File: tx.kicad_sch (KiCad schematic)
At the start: 58 parts, among them Q10 MMBF170, Q11 MMBF170, Q12 MMBF170, Q13 MMBF170, Q2 MMBF170, Q3 MMBF170, Q4 MMBF170, Q5 MMBF170, Q6 MMBF170, Q7 MMBF170, Q8 MMBF170, Q9 MMBF170, T1 BN-43-202_DualPri_CTSec, U4 ICE40UP5K-SG48ITR, U5 TLV70012, U6 CD74ACT541M96G4

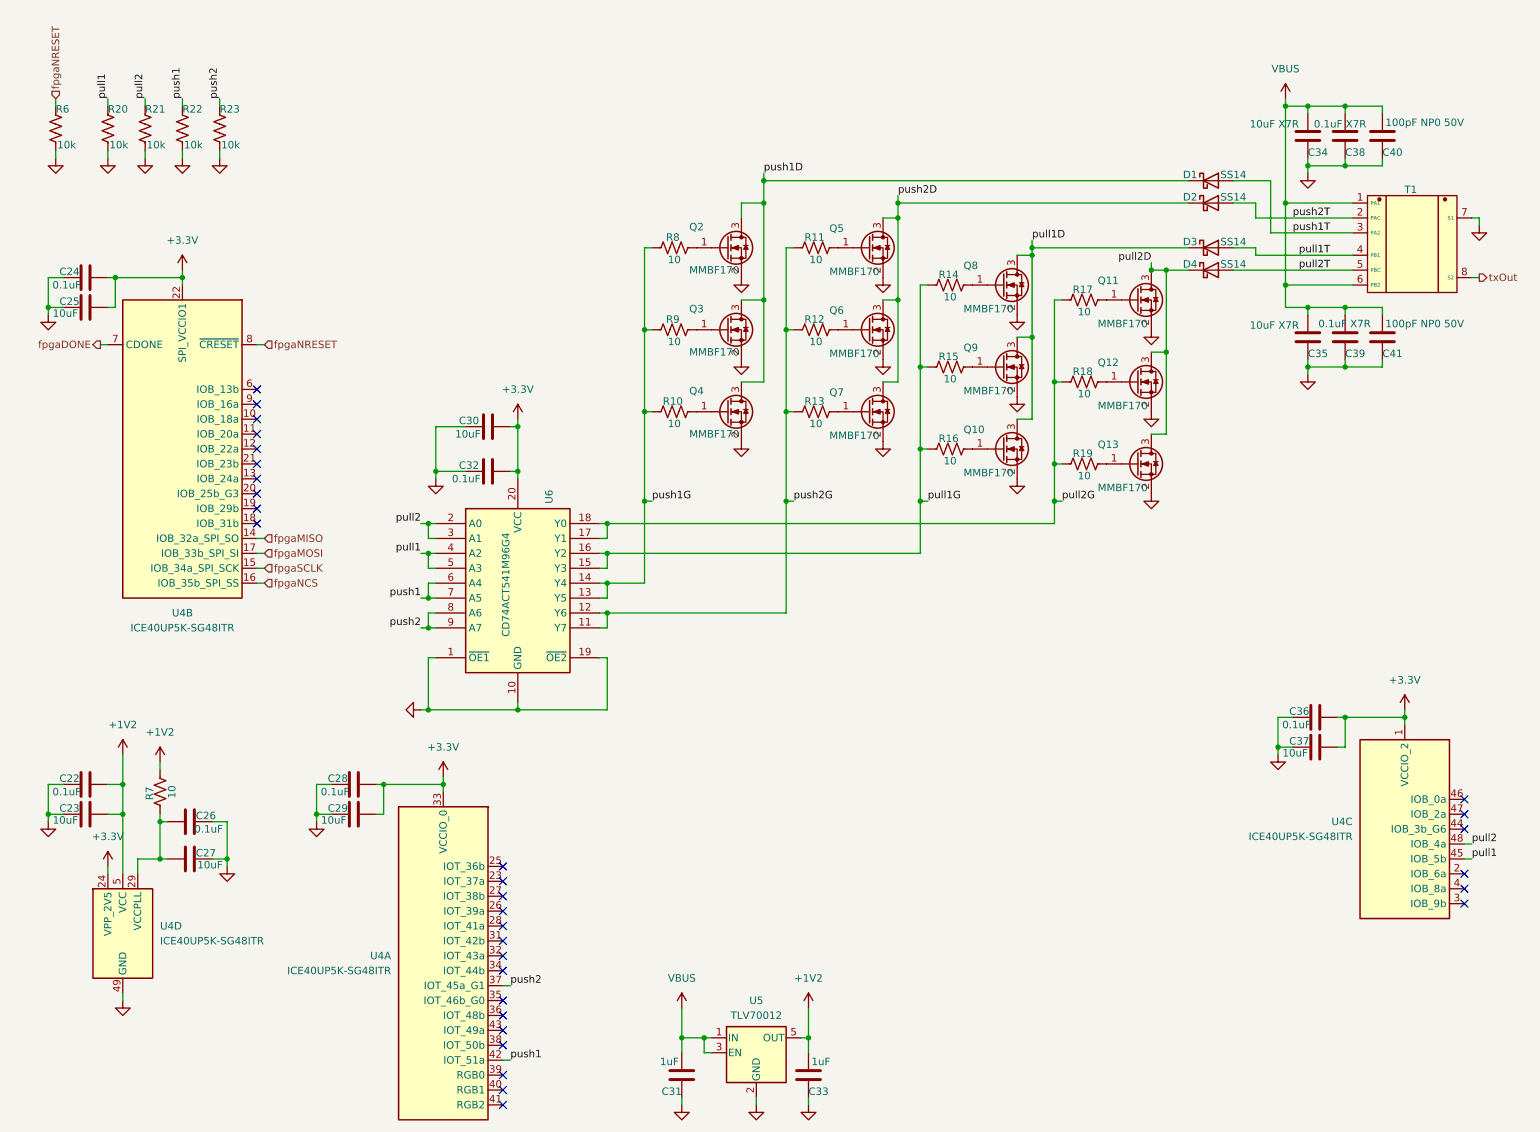
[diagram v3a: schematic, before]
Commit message: Submitted to PCBway (I had to update BOM after oops)
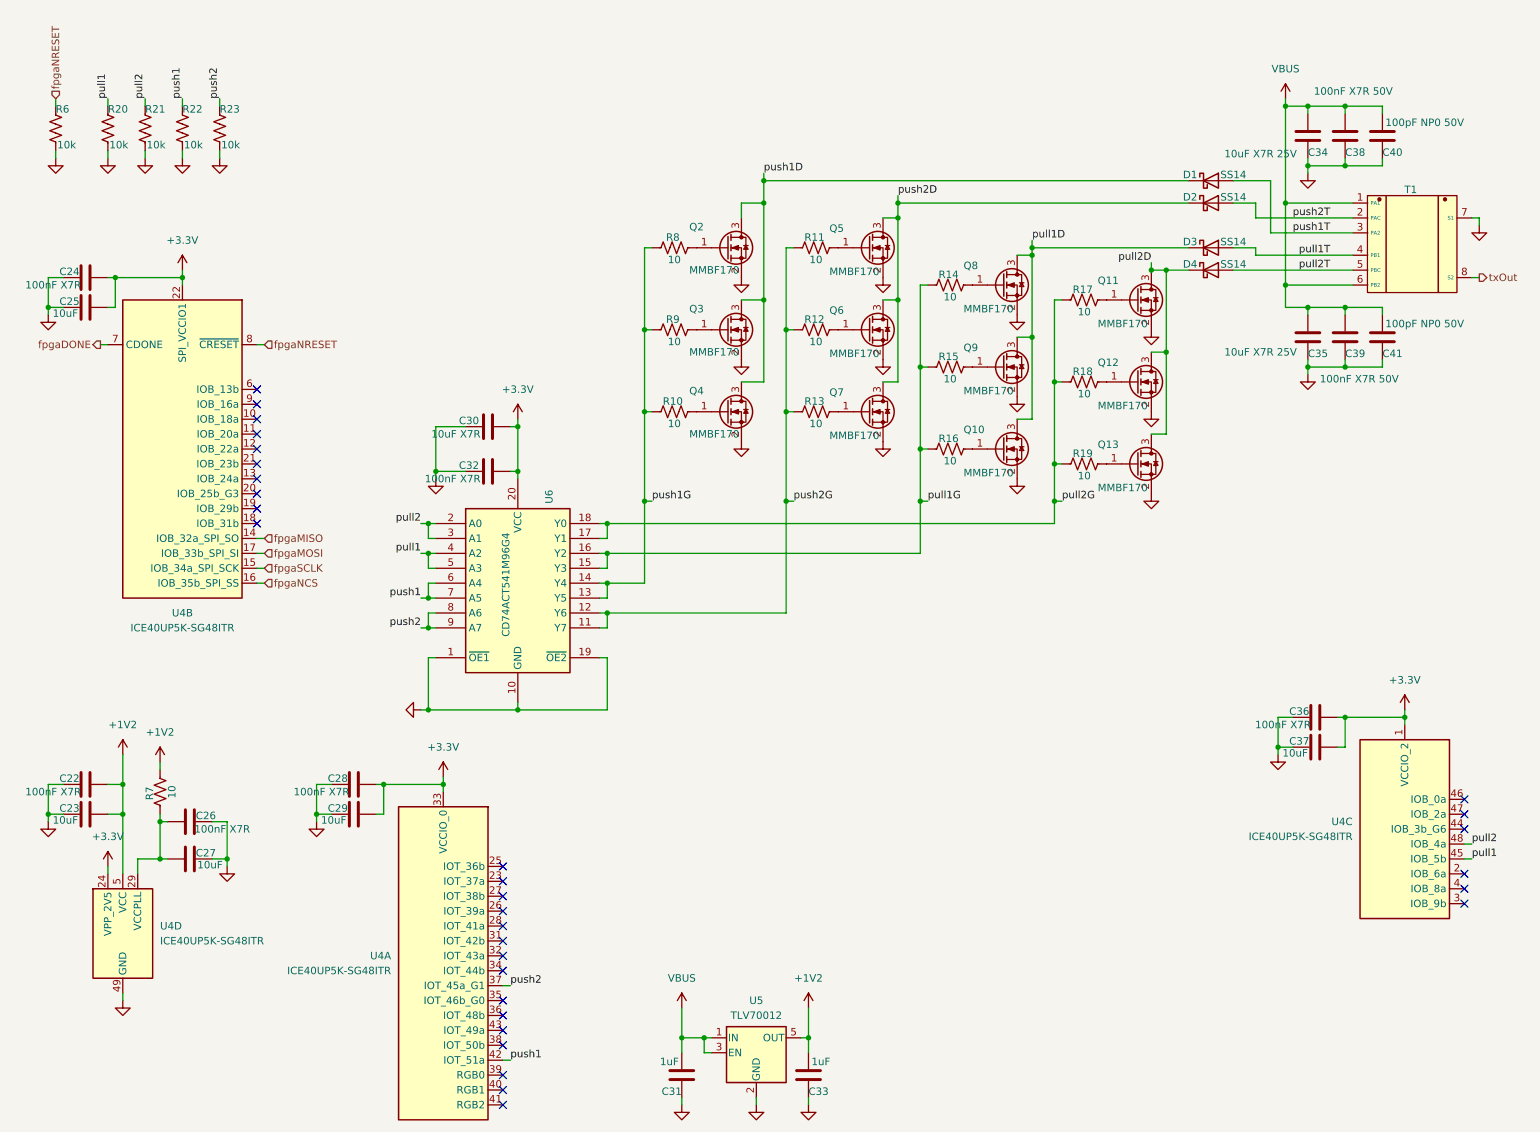
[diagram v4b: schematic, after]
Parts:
- C22, C24, C26, C28, C32, C36: value 0.1uF -> 100nF X7R; LCSC (none) -> C14663
- C23, C25, C27, C29, C37: LCSC (none) -> C2959727
- C30: value 10uF -> 10uF X7R; LCSC (none) -> C32635
- C31, C33: LCSC (none) -> C29936
- C34, C35: value 10uF X7R -> 10uF X7R 25V; LCSC (none) -> C96446
- C38, C39: value 0.1uF X7R -> 100nF X7R 50V; LCSC (none) -> C14663
- C40, C41: LCSC (none) -> C14665
- D1, D2, D3, D4: LCSC (none) -> C83852
- R10, R11, R12, R13, R14, R15, R16, R17, R18, R19, R7, R8, R9: LCSC (none) -> C2907091
- R20, R21, R22, R23, R6: LCSC (none) -> C2930027
- T1: LCSC (none) -> C7174817; MFG (none) -> Fair-Rite; MPN (none) -> 2843000202
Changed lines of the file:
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@@
 			)
 		)
-		(property "Value" "0.1uF"
+		(property "Value" "100nF X7R"
 			(at 20.828 58.42 90)
 			(effects
@@
 			)
 		)
-		(property "LCSC" ""
+		(property "LCSC" "C14663"
 			(at 21.59 57.15 90)
 			(effects
@@
 			)
 		)
-		(property "LCSC" ""
+		(property "LCSC" "C2907091"
 			(at 146.05 80.01 90)
 			(effects
@@
 			)
 		)
-		(property "LCSC" ""
+		(property "LCSC" "C83852"
 			(at 213.36 40.64 0)
 			(effects
@@
 			)
 		)
-		(property "LCSC" ""
+		(property "LCSC" "C83852"
 			(at 213.36 52.07 0)
 			(effects
@@
 			)
 		)
-		(property "LCSC" ""
+		(property "LCSC" "C2907091"
 			(at 146.05 66.04 90)
 			(effects
@@
 			)
 		)
-		(property "LCSC" ""
+		(property "LCSC" "C2907091"
 			(at 121.92 66.04 90)
 			(effects
@@
 			)
 		)
-		(property "Value" "0.1uF"
+		(property "Value" "100nF X7R"
 			(at 88.9 91.44 90)
 			(effects
@@
 			)
 		)
-		(property "LCSC" ""
+		(property "LCSC" "C14663"
 			(at 90.17 90.17 0)
 			(effects
@@
 			)
 		)
-		(property "LCSC" ""
+		(property "LCSC" "C29936"
 			(at 144.78 193.04 0)
 			(effects
@@
 			)
 		)
-		(property "LCSC" ""
+		(property "LCSC" "C2930027"
 			(at 44.45 31.75 0)
 			(effects
@@
 			)
 		)
-		(property "LCSC" ""
+		(property "LCSC" "C2930027"
 			(at 38.1 31.75 0)
 			(effects
@@
 			)
 		)
-		(property "Value" "10uF X7R"
-			(at 219.964 30.988 0)
+		(property "Value" "10uF X7R 25V"
+			(at 215.646 36.068 0)
 			(effects
 				(font
@@
 			)
 		)
-		(property "LCSC" ""
+		(property "LCSC" "C96446"
 			(at 229.87 33.02 0)
 			(effects
@@
 			)
 		)
-		(property "LCSC" ""
+		(property "LCSC" "C2930027"
 			(at 31.75 31.75 0)
 			(effects
@@
 			)
 		)
-		(property "LCSC" ""
+		(property "LCSC" "C29936"
 			(at 123.19 193.04 0)
 			(effects
@@
 			)
 		)
-		(property "LCSC" ""
+		(property "LCSC" "C2959727"
 			(at 21.59 148.59 90)
 			(effects
@@
 			)
 		)
-		(property "LCSC" ""
+		(property "LCSC" "C14665"
 			(at 242.57 67.31 0)
 			(effects
@@
 			)
 		)
-		(property "LCSC" ""
+		(property "LCSC" "C2907091"
 			(at 191.77 60.96 90)
 			(effects
@@
 			)
 		)
-		(property "LCSC" ""
+		(property "LCSC" "C2959727"
 			(at 39.37 156.21 90)
 			(effects
@@
 			)
 		)
-		(property "Value" "0.1uF"
+		(property "Value" "100nF X7R"
 			(at 230.378 133.35 90)
 			(effects
@@
 			)
 		)
-		(property "LCSC" ""
+		(property "LCSC" "C14663"
 			(at 231.14 132.08 90)
 			(effects
@@
 			)
 		)
-		(property "Value" "0.1uF X7R"
-			(at 230.886 30.988 0)
+		(property "Value" "100nF X7R 50V"
+			(at 230.886 25.4 0)
 			(effects
 				(font
@@
 			)
 		)
-		(property "LCSC" ""
+		(property "LCSC" "C14663"
 			(at 236.22 33.02 0)
 			(effects
@@
 			)
 		)
-		(property "LCSC" ""
+		(property "LCSC" "C2907091"
 			(at 191.77 74.93 90)
 			(effects
@@
 			)
 		)
-		(property "LCSC" ""
+		(property "LCSC" "C2907091"
 			(at 121.92 52.07 90)
 			(effects
@@
 			)
 		)
-		(property "LCSC" ""
+		(property "LCSC" "C7174817"
+			(at 247.65 49.53 0)
+			(effects
+				(font
+					(size 1.27 1.27)
+				)
+				(hide yes)
+			)
+		)
+		(property "MFG" "Fair-Rite"
+			(at 247.65 49.53 0)
+			(effects
+				(font
+					(size 1.27 1.27)
+				)
+				(hide yes)
+			)
+		)
+		(property "MPN" "2843000202"
 			(at 247.65 49.53 0)
 			(effects
@@
 			)
 		)
-		(property "Value" "10uF X7R"
-			(at 219.964 65.278 0)
+		(property "Value" "10uF X7R 25V"
+			(at 215.646 69.85 0)
 			(effects
 				(font
@@
 			)
 		)
-		(property "LCSC" ""
+		(property "LCSC" "C96446"
 			(at 229.87 67.31 0)
 			(effects
@@
 			)
 		)
-		(property "Value" "0.1uF"
+		(property "Value" "100nF X7R"
 			(at 66.548 144.78 90)
 			(effects
@@
 			)
 		)
-		(property "LCSC" ""
+		(property "LCSC" "C14663"
 			(at 67.31 143.51 90)
 			(effects
@@
 			)
 		)
-		(property "LCSC" ""
+		(property "LCSC" "C2959727"
 			(at 67.31 148.59 90)
 			(effects
@@
 			)
 		)
-		(property "LCSC" ""
+		(property "LCSC" "C2930027"
 			(at 16.51 31.75 0)
 			(effects
@@
 			)
 		)
-		(property "Value" "0.1uF X7R"
-			(at 231.648 65.024 0)
+		(property "Value" "100nF X7R 50V"
+			(at 231.902 74.422 0)
 			(effects
 				(font
@@
 			)
 		)
-		(property "LCSC" ""
+		(property "LCSC" "C14663"
 			(at 236.22 67.31 0)
 			(effects
@@
 			)
 		)
-		(property "LCSC" ""
+		(property "LCSC" "C2907091"
 			(at 121.92 80.01 90)
 			(effects
@@
 			)
 		)
-		(property "LCSC" ""
+		(property "LCSC" "C2907091"
 			(at 191.77 88.9 90)
 			(effects
@@
 			)
 		)
-		(property "LCSC" ""
+		(property "LCSC" "C2959727"
 			(at 21.59 62.23 90)
 			(effects
@@
 			)
 		)
-		(property "LCSC" ""
+		(property "LCSC" "C14665"
 			(at 242.57 33.02 0)
 			(effects
@@
 			)
 		)
-		(property "LCSC" ""
+		(property "LCSC" "C83852"
 			(at 213.36 55.88 0)
 			(effects
@@
 			)
 		)
-		(property "LCSC" ""
+		(property "LCSC" "C83852"
 			(at 213.36 44.45 0)
 			(effects
@@
 			)
 		)
-		(property "Value" "0.1uF"
+		(property "Value" "100nF X7R"
 			(at 20.828 144.78 90)
 			(effects
@@
 			)
 		)
-		(property "LCSC" ""
+		(property "LCSC" "C14663"
 			(at 21.59 143.51 90)
 			(effects
@@
 			)
 		)
-		(property "Value" "0.1uF"
+		(property "Value" "100nF X7R"
 			(at 40.132 151.13 90)
 			(effects
@@
 			)
 		)
-		(property "LCSC" ""
+		(property "LCSC" "C14663"
 			(at 39.37 149.86 90)
 			(effects
@@
 			)
 		)
-		(property "LCSC" ""
+		(property "LCSC" "C2907091"
 			(at 168.91 58.42 90)
 			(effects
@@
 			)
 		)
-		(property "LCSC" ""
+		(property "LCSC" "C2930027"
 			(at 25.4 31.75 0)
 			(effects
@@
 			)
 		)
-		(property "LCSC" ""
+		(property "LCSC" "C2959727"
 			(at 231.14 137.16 90)
 			(effects
@@
 			)
 		)
-		(property "LCSC" ""
+		(property "LCSC" "C2907091"
 			(at 168.91 72.39 90)
 			(effects
@@
 			)
 		)
-		(property "LCSC" ""
+		(property "LCSC" "C2907091"
 			(at 146.05 52.07 90)
 			(effects
@@
 			)
 		)
-		(property "LCSC" ""
+		(property "LCSC" "C2907091"
 			(at 168.91 86.36 90)
 			(effects
@@
 			)
 		)
-		(property "Value" "10uF"
+		(property "Value" "10uF X7R"
 			(at 88.9 83.82 90)
 			(effects
@@
 			)
 		)
-		(property "LCSC" ""
+		(property "LCSC" "C32635"
 			(at 90.17 82.55 0)
 			(effects
@@
 			)
 		)
-		(property "LCSC" ""
+		(property "LCSC" "C2907091"
 			(at 34.29 144.78 90)
 			(effects

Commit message: Cleanup. Better USB diff pair with 0ohm and TVS as recommended. Return to rectangular outline and even smaller. Mounting holes are consistently placed relative to board corners.
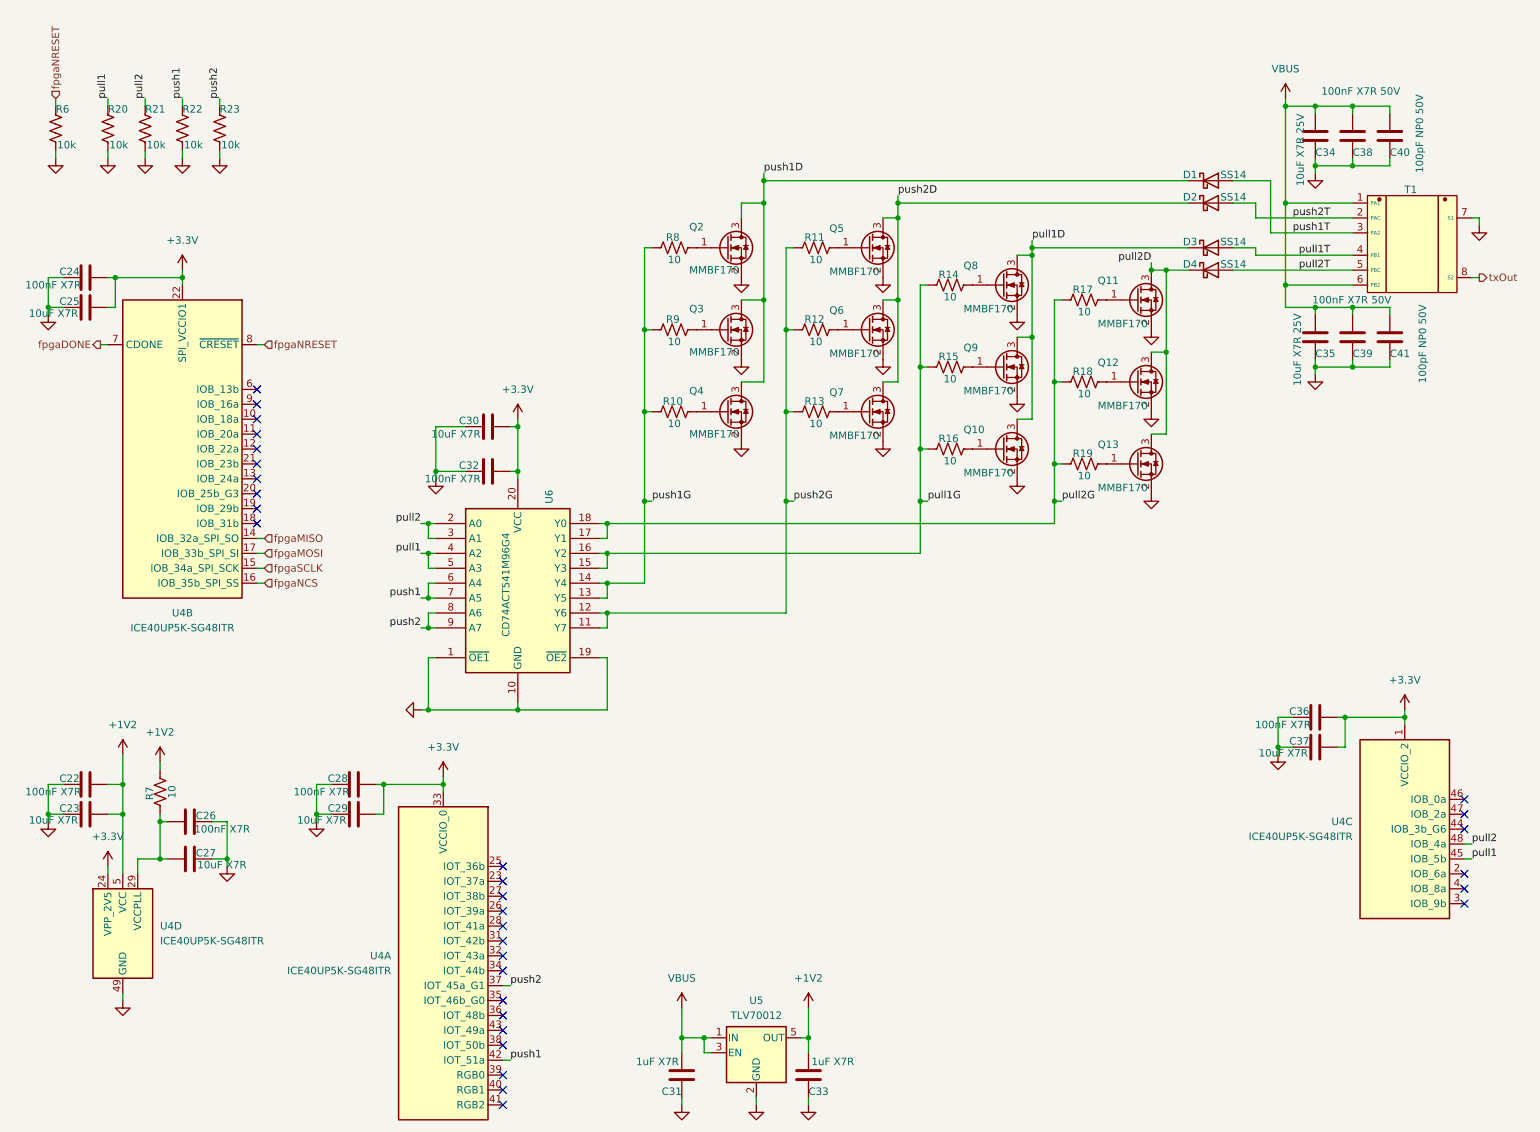
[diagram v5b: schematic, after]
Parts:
- C23, C25, C27, C29, C37: value 10uF -> 10uF X7R
- C31, C33: value 1uF -> 1uF X7R
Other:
- moved on the sheet: C34, C35, C38, C39, C40, C41

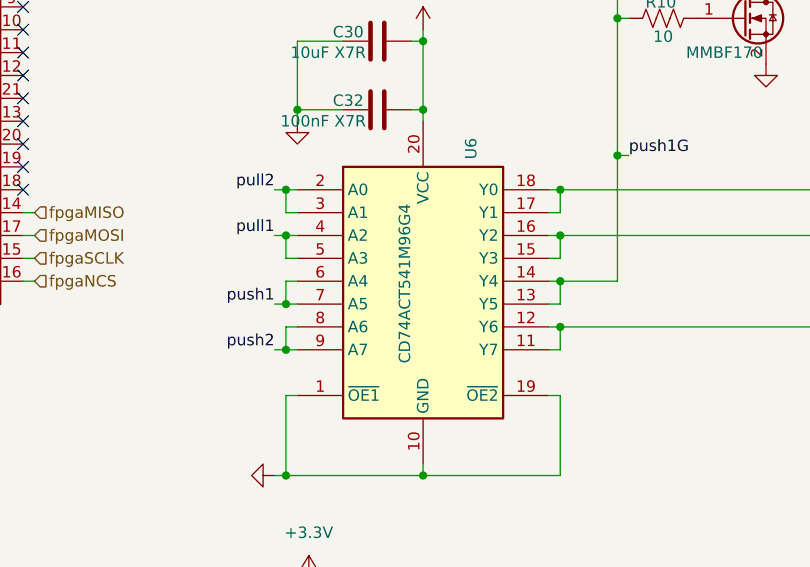
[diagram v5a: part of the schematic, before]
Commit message: Switch to SSOP package for 74ACT541. Tweak a bunch of layout for DFM and maybe some improved SI.
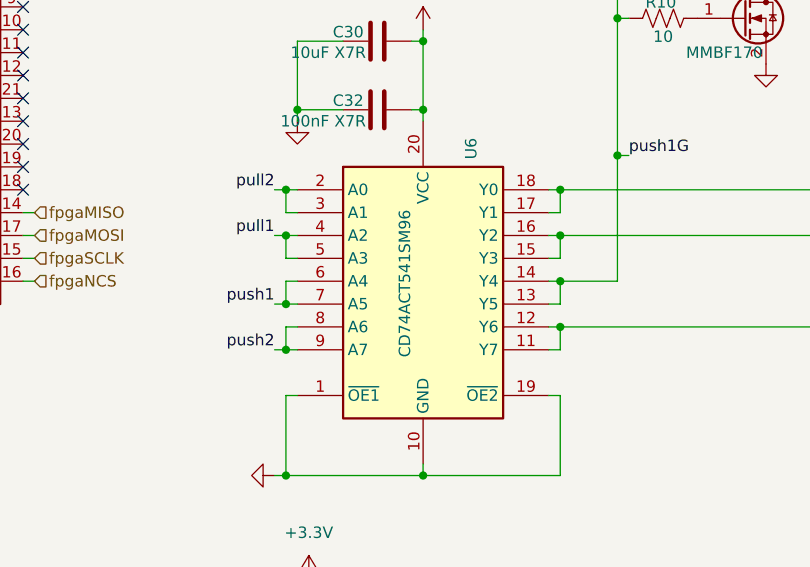
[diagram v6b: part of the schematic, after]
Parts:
- U6: value CD74ACT541M96G4 -> CD74ACT541SM96; footprint SOIC127P1030X265-20N -> Library:SOP65P780X200-20N; LCSC C899000 -> (none); MPN 74ACT541SCX -> (none); Manufacturer_Name onsemi -> (none); Manufacturer_Part_Number CD74ACT541M96G4 -> (none); Mouser Part Number 74ACT541SCX -> (none); Mouser Price/Stock https://www.lcsc.com/datasheet/C899000.pdf -> (none)
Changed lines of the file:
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@@
 			)
 		)
-		(property "Value" "CD74ACT541M96G4"
+		(property "Value" "CD74ACT541SM96"
 			(at 93.218 109.474 90)
 			(effects
@@
 			)
 		)
-		(property "Footprint" "SOIC127P1030X265-20N"
+		(property "Footprint" "Library:SOP65P780X200-20N"
 			(at 105.41 193.98 0)
 			(effects
@@
 			)
 		)
-		(property "Datasheet" "https://www.arrow.com/en/products/cd74act541m96g4/texas-instruments"
+		(property "Datasheet" "https://www.ti.com/lit/gpn/cd74act541"
 			(at 105.41 293.98 0)
 			(effects
@@
 			)
 		)
-		(property "Description" "Buffer/Line Driver 8-CH Non-Inverting 3-ST CMOS 20-Pin SOIC T/R"
+		(property "Description" "Buffer/Line Driver 8-CH Non-Inverting 3-ST CMOS 20-Pin SSOP T/R"
 			(at 81.28 99.06 0)
 			(effects
@@
 				(hide yes)
 			)
-		)
-		(property "Mouser Part Number" "74ACT541SCX"
-			(at 105.41 593.98 0)
-			(effects
-				(font
-					(size 1.27 1.27)
-				)
-				(justify left top)
-				(hide yes)
-			)
-		)
-		(property "Mouser Price/Stock" "https://www.lcsc.com/datasheet/C899000.pdf"
-			(at 105.41 693.98 0)
-			(effects
-				(font
-					(size 1.27 1.27)
-				)
-				(justify left top)
-				(hide yes)
-			)
-		)
-		(property "Manufacturer_Name" "onsemi"
-			(at 105.41 793.98 0)
-			(effects
-				(font
-					(size 1.27 1.27)
-				)
-				(justify left top)
-				(hide yes)
-			)
-		)
-		(property "Manufacturer_Part_Number" "CD74ACT541M96G4"
-			(at 105.41 893.98 0)
-			(effects
-				(font
-					(size 1.27 1.27)
-				)
-				(justify left top)
-				(hide yes)
-			)
-		)
-		(property "LCSC" "C899000"
-			(at 95.25 104.14 90)
-			(effects
-				(font
-					(size 1.27 1.27)
-				)
-				(hide yes)
-			)
-		)
-		(property "MPN" "74ACT541SCX"
-			(at 95.25 104.14 90)
-			(effects
-				(font
-					(size 1.27 1.27)
-				)
-				(hide yes)
-			)
